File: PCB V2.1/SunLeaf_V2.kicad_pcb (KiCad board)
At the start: 4 copper layers, 77.5 x 40 mm, 121 parts, among them IC1 ESP_09, J1 20021121-00010C4LF, J10 B4B-PH-K-S(LF)(SN), J11 B4B-PH-K-S(LF)(SN), J12 B4B-PH-K-S(LF)(SN), J13 B4B-PH-K-S(LF)(SN), J14 B4B-PH-K-S(LF)(SN), J15 B4B-PH-K-S(LF)(SN), J16 B4B-PH-K-S(LF)(SN), J2 0475890001-MicroUSBPort, J3 B2B-PH-K-S(LF)(SN), J4 B3B-PH-K-S(LF)(SN), J5 B4B-PH-K-S(LF)(SN), J6 B4B-PH-K-S(LF)(SN), J7 B4B-PH-K-S(LF)(SN), J8 B4B-PH-K-S(LF)(SN), J9 B4B-PH-K-S(LF)(SN), P1 CONN_01X04, P2 CONN_01X03, Q1 DMG2307L-7, Q2 DMG2307L-7, SW1 B3U-1000P, SW2 B3U-1000P, T1 1909763-1, U1 STM32F446RET6_-_TQFP64, U2 BQ24210DQCT, U3 AZ1117CR-3.3TRG1_1, U4 74HC4052D, U5 PCA9518DBQR, X1 ABM3B8.000MHZB2T, X2 ABS07-32.768KHZ-9-T

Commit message: Schematic Changes
Schematic changes saved.
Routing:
- net (no net): track 30.7 -> 0.00 mm, vias 10 -> 0
- net GND: track 256.5 -> 275.0 mm, vias 130 -> 141
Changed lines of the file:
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@@
     (links 309)
     (no_connects 7)
-    (area 42.949999 29.949999 120.550001 70.050001)
+    (area 21.000001 17.300001 134.897448 87.526447)
     (thickness 1.6)
     (drawings 165)
-    (tracks 1376)
+    (tracks 1365)
     (zones 0)
     (modules 121)
@@
     (40 Dwgs.User user)
     (41 Cmts.User user)
-    (42 Eco1.User user hide)
+    (42 Eco1.User user)
     (43 Eco2.User user)
     (44 Edge.Cuts user)
@@
   (gr_line (start 120.5 30) (end 43 30) (layer Edge.Cuts) (width 0.1))
   (gr_line (start 120.5 30) (end 120.5 70) (layer Edge.Cuts) (width 0.1))
-  (segment (start 77.597 61.214) (end 77.597 61.86384) (width 0.1778) (layer F.Cu) (net 0))
-  (segment (start 77.597 61.86384) (end 76.232752 63.228088) (width 0.1778) (layer F.Cu) (net 0))
-  (segment (start 79.248 58.039) (end 78.359 58.039) (width 0.1778) (layer F.Cu) (net 0))
-  (via (at 79.248 58.039) (size 0.635) (drill 0.3302) (layers F.Cu B.Cu) (net 0))
-  (segment (start 77.597 59.182) (end 77.597 58.801) (width 0.1778) (layer F.Cu) (net 0))
-  (segment (start 77.597 58.801) (end 78.359 58.039) (width 0.1778) (layer F.Cu) (net 0))
-  (via (at 78.359 58.039) (size 0.635) (drill 0.3302) (layers F.Cu B.Cu) (net 0))
-  (segment (start 78.359 60.325) (end 78.359 60.452) (width 0.1778) (layer F.Cu) (net 0))
-  (segment (start 78.359 60.452) (end 77.597 61.214) (width 0.1778) (layer F.Cu) (net 0))
-  (segment (start 79.375 60.325) (end 78.359 60.325) (width 0.1778) (layer F.Cu) (net 0))
-  (via (at 79.375 60.325) (size 0.635) (drill 0.3302) (layers F.Cu B.Cu) (net 0))
-  (via (at 78.359 60.325) (size 0.635) (drill 0.3302) (layers F.Cu B.Cu) (net 0))
-  (segment (start 75.438 54.991) (end 75.438 55.118) (width 0.1778) (layer F.Cu) (net 0))
-  (segment (start 75.438 55.118) (end 76.327 56.007) (width 0.1778) (layer F.Cu) (net 0))
-  (segment (start 75.438 53.975) (end 75.438 54.991) (width 0.1778) (layer F.Cu) (net 0))
-  (via (at 75.438 53.975) (size 0.635) (drill 0.3302) (layers F.Cu B.Cu) (net 0))
-  (via (at 75.438 54.991) (size 0.635) (drill 0.3302) (layers F.Cu B.Cu) (net 0))
-  (segment (start 73.152 54.991) (end 73.152 54.102) (width 0.1778) (layer B.Cu) (net 0))
-  (via (at 73.152 54.102) (size 0.635) (drill 0.3302) (layers F.Cu B.Cu) (net 0))
-  (segment (start 74.295 56.007) (end 74.168 56.007) (width 0.1778) (layer F.Cu) (net 0))
-  (segment (start 74.168 56.007) (end 73.152 54.991) (width 0.1778) (layer F.Cu) (net 0))
-  (via (at 73.152 54.991) (size 0.635) (drill 0.3302) (layers F.Cu B.Cu) (net 0))
-  (segment (start 70.811612 54.864) (end 70.811612 53.99643) (width 0.1778) (layer B.Cu) (net 0))
-  (via (at 70.811612 53.99643) (size 0.635) (drill 0.3302) (layers F.Cu B.Cu) (net 0))
-  (segment (start 71.12 57.15) (end 71.12 55.172388) (width 0.1778) (layer F.Cu) (net 0))
-  (segment (start 71.12 55.172388) (end 70.811612 54.864) (width 0.1778) (layer F.Cu) (net 0))
-  (via (at 70.811612 54.864) (size 0.635) (drill 0.3302) (layers F.Cu B.Cu) (net 0))
-  (segment (start 77.597 59.182) (end 77.597 59.631012) (width 0.1778) (layer F.Cu) (net 0))
-  (segment (start 77.597 59.631012) (end 77.597 61.214) (width 0.1778) (layer F.Cu) (net 0))
-  (segment (start 77.597 57.15) (end 77.47 57.15) (width 0.1778) (layer F.Cu) (net 0))
-  (segment (start 77.47 57.15) (end 76.327 56.007) (width 0.1778) (layer F.Cu) (net 0))
-  (segment (start 72.263 56.388) (end 73.914 56.388) (width 0.1778) (layer F.Cu) (net 0))
-  (segment (start 73.914 56.388) (end 74.295 56.007) (width 0.1778) (layer F.Cu) (net 0))
-  (segment (start 71.12 59.182) (end 71.12 57.15) (width 0.1778) (layer F.Cu) (net 0))
-  (segment (start 71.12 59.182) (end 71.12 61.087) (width 0.1778) (layer F.Cu) (net 0))
-  (segment (start 72.263 56.388) (end 71.882 56.388) (width 0.1778) (layer F.Cu) (net 0))
-  (segment (start 71.882 56.388) (end 71.12 57.15) (width 0.1778) (layer F.Cu) (net 0))
-  (segment (start 76.327 56.007) (end 74.295 56.007) (width 0.1778) (layer F.Cu) (net 0))
-  (segment (start 77.597 59.182) (end 77.597 57.15) (width 0.1778) (layer F.Cu) (net 0))
   (via (at 61.671682 53.343897) (size 0.635) (drill 0.3302) (layers F.Cu B.Cu) (net 1))
   (segment (start 61.7474 53.8476) (end 61.7474 53.419615) (width 0.1778) (layer F.Cu) (net 1))
@@
   (segment (start 54.0004 66.8528) (end 54.356 66.4972) (width 0.1778) (layer F.Cu) (net 1))
   (via (at 54.356 66.4972) (size 0.635) (drill 0.3302) (layers F.Cu B.Cu) (net 1))
+  (segment (start 72.284225 57.184946) (end 71.281946 57.184946) (width 0.1778) (layer F.Cu) (net 2))
+  (segment (start 71.281946 57.184946) (end 71.247 57.15) (width 0.1778) (layer F.Cu) (net 2))
+  (via (at 71.247 57.15) (size 0.635) (drill 0.3302) (layers F.Cu B.Cu) (net 2))
+  (segment (start 70.993 55.245) (end 70.993 54.102) (width 0.1778) (layer B.Cu) (net 2))
+  (via (at 70.993 54.102) (size 0.635) (drill 0.3302) (layers F.Cu B.Cu) (net 2))
+  (segment (start 72.284225 57.184946) (end 70.993 55.893721) (width 0.1778) (layer F.Cu) (net 2))
+  (segment (start 70.993 55.893721) (end 70.993 55.245) (width 0.1778) (layer F.Cu) (net 2))
+  (via (at 70.993 55.245) (size 0.635) (drill 0.3302) (layers F.Cu B.Cu) (net 2))
+  (segment (start 73.152 54.229) (end 73.152 55.626) (width 0.1778) (layer F.Cu) (net 2))
+  (via (at 73.152 54.229) (size 0.635) (drill 0.3302) (layers F.Cu B.Cu) (net 2))
+  (segment (start 74.25226 57.166251) (end 73.152 56.065991) (width 0.1778) (layer F.Cu) (net 2))
+  (segment (start 73.152 56.065991) (end 73.152 55.626) (width 0.1778) (layer F.Cu) (net 2))
+  (via (at 73.152 55.626) (size 0.635) (drill 0.3302) (layers F.Cu B.Cu) (net 2))
+  (segment (start 75.438 53.975) (end 75.438 55.245) (width 0.1778) (layer F.Cu) (net 2))
+  (via (at 75.438 53.975) (size 0.635) (drill 0.3302) (layers F.Cu B.Cu) (net 2))
+  (segment (start 76.265361 57.161389) (end 76.265361 56.072361) (width 0.1778) (layer F.Cu) (net 2))
+  (segment (start 76.265361 56.072361) (end 75.438 55.245) (width 0.1778) (layer F.Cu) (net 2))
+  (via (at 75.438 55.245) (size 0.635) (drill 0.3302) (layers F.Cu B.Cu) (net 2))
+  (segment (start 79.121 58.166) (end 78.232 58.166) (width 0.1778) (layer F.Cu) (net 2))
+  (via (at 79.121 58.166) (size 0.635) (drill 0.3302) (layers F.Cu B.Cu) (net 2))
+  (segment (start 76.265361 57.161389) (end 77.227389 57.161389) (width 0.1778) (layer F.Cu) (net 2))
+  (segment (start 77.227389 57.161389) (end 78.232 58.166) (width 0.1778) (layer F.Cu) (net 2))
+  (via (at 78.232 58.166) (size 0.635) (drill 0.3302) (layers F.Cu B.Cu) (net 2))
+  (segment (start 79.502 60.198) (end 78.359 60.198) (width 0.1778) (layer F.Cu) (net 2))
+  (via (at 79.502 60.198) (size 0.635) (drill 0.3302) (layers F.Cu B.Cu) (net 2))
+  (segment (start 76.274175 61.192843) (end 77.364157 61.192843) (width 0.1778) (layer F.Cu) (net 2))
+  (segment (start 77.364157 61.192843) (end 78.359 60.198) (width 0.1778) (layer F.Cu) (net 2))
+  (via (at 78.359 60.198) (size 0.635) (drill 0.3302) (layers F.Cu B.Cu) (net 2))
   (segment (start 80.518 62.992) (end 79.112 64.398) (width 0.1778) (layer F.Cu) (net 2))
   (segment (start 79.112 64.398) (end 79.0601 64.398) (width 0.1778) (layer F.Cu) (net 2))

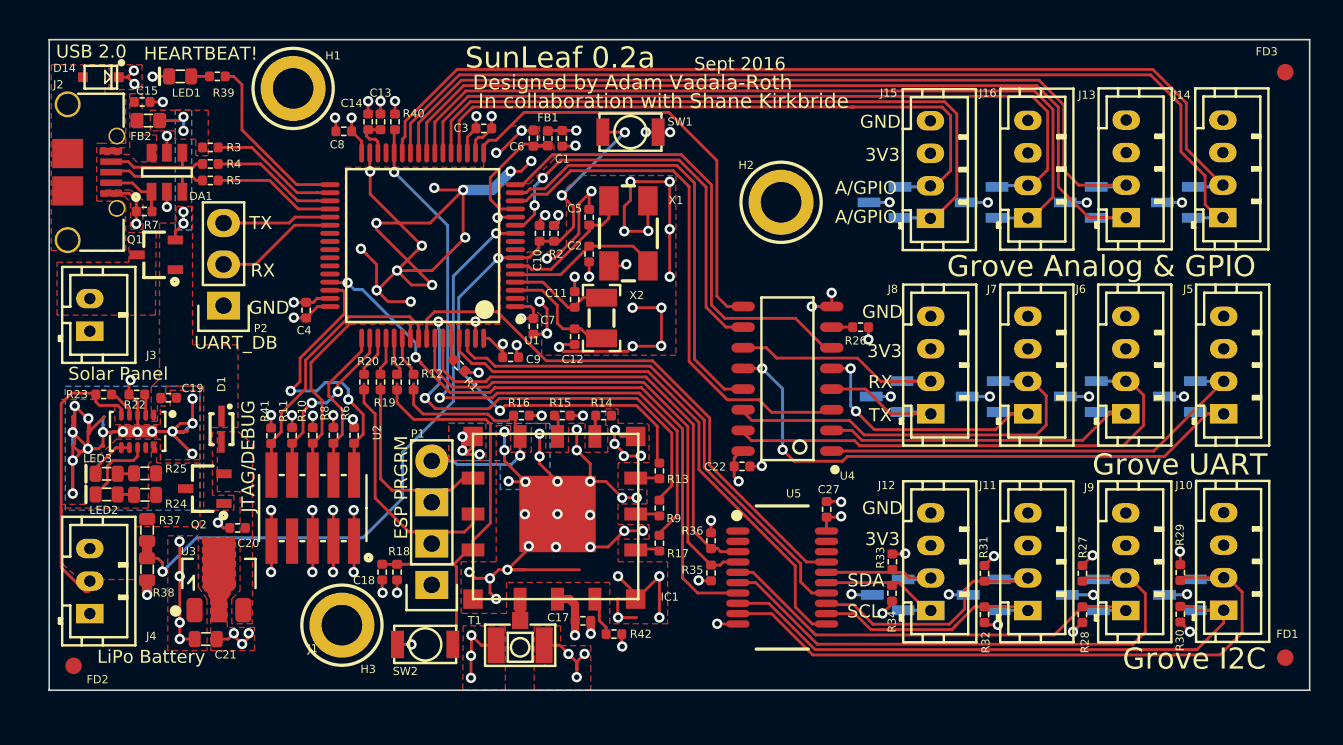
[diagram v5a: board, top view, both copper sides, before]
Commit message: Test Points
Test points added as well as some retooling of the PCB overall. More
updates to come before the pending fab
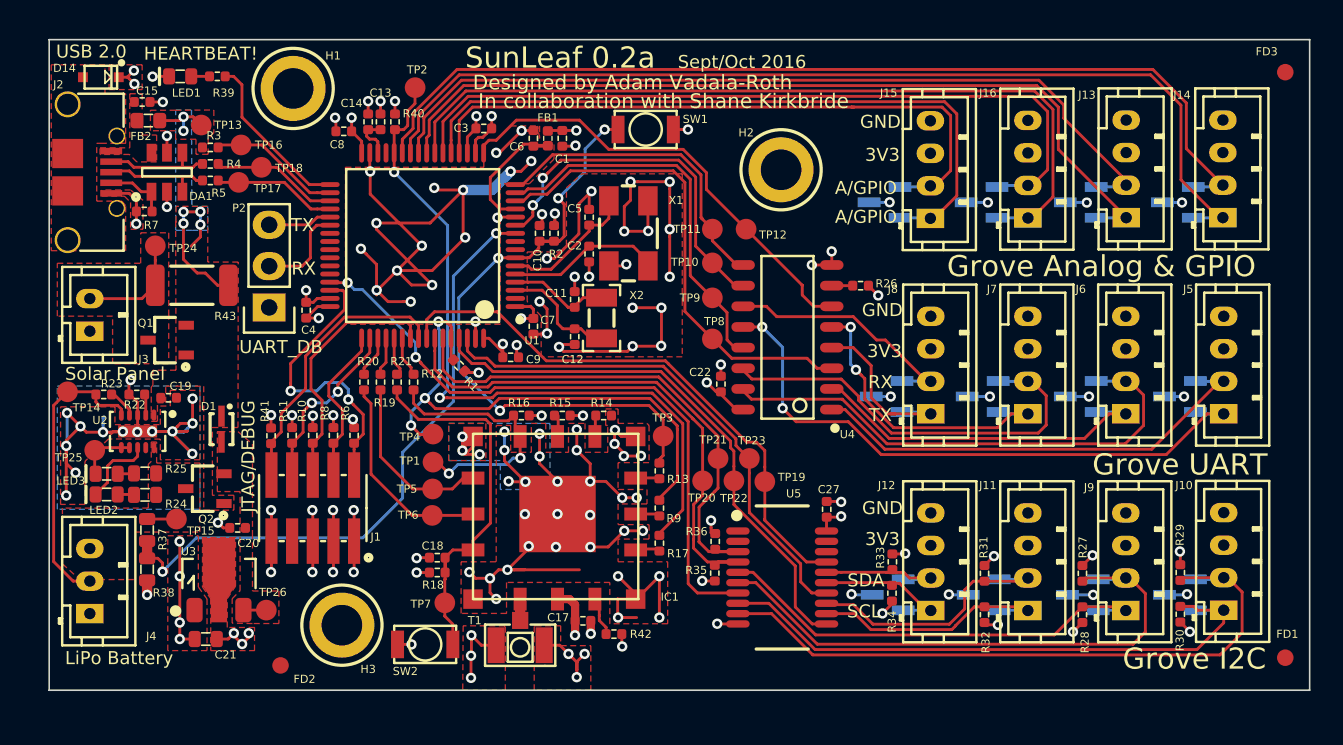
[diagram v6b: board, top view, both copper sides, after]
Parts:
- removed P1: CONN_01X04, Pin_Headers:Pin_Header_Straight_1x04
- added R43: RC5025J000CS, PCB_Footprints:R2010, F.Cu at (51.8, 45.1)
- added TP1: TEST_POINT, PCB_Footprints:TEST_POINT, F.Cu at (66.6, 56.0)
- added TP10: TEST_POINT, PCB_Footprints:TEST_POINT, F.Cu at (83.8, 43.7)
- added TP11: TEST_POINT, PCB_Footprints:TEST_POINT, F.Cu at (83.8, 41.6)
- added TP12: TEST_POINT, PCB_Footprints:TEST_POINT, F.Cu at (85.8, 41.6)
- added TP13: TEST_POINT, PCB_Footprints:TEST_POINT, F.Cu at (52.4, 35.2)
- added TP14: TEST_POINT, PCB_Footprints:TEST_POINT, F.Cu at (44.1, 51.6)
- added TP15: TEST_POINT, PCB_Footprints:TEST_POINT, F.Cu at (50.8, 59.5)
- added TP16: TEST_POINT, PCB_Footprints:TEST_POINT, F.Cu at (54.8, 36.5)
- added TP17: TEST_POINT, PCB_Footprints:TEST_POINT, F.Cu at (54.6, 38.8)
- added TP18: TEST_POINT, PCB_Footprints:TEST_POINT, F.Cu at (56.0, 37.9)
- added TP19: TEST_POINT, PCB_Footprints:TEST_POINT, F.Cu at (87.0, 57.2)
- added TP2: TEST_POINT, PCB_Footprints:TEST_POINT, F.Cu at (65.5, 33.0)
- added TP20: TEST_POINT, PCB_Footprints:TEST_POINT, F.Cu at (83.2, 57.1)
- added TP21: TEST_POINT, PCB_Footprints:TEST_POINT, F.Cu at (84.1, 55.8)
- added TP22: TEST_POINT, PCB_Footprints:TEST_POINT, F.Cu at (85.1, 57.1)
- added TP23: TEST_POINT, PCB_Footprints:TEST_POINT, F.Cu at (86.0, 55.8)
- added TP24: TEST_POINT, PCB_Footprints:TEST_POINT, F.Cu at (49.5, 42.7)
- added TP25: TEST_POINT, PCB_Footprints:TEST_POINT, F.Cu at (45.8, 55.2)
- added TP26: TEST_POINT, PCB_Footprints:TEST_POINT, F.Cu at (56.4, 65.1)
- added TP3: TEST_POINT, PCB_Footprints:TEST_POINT, F.Cu at (80.8, 54.4)
- added TP4: TEST_POINT, PCB_Footprints:TEST_POINT, F.Cu at (66.6, 54.2)
- added TP5: TEST_POINT, PCB_Footprints:TEST_POINT, F.Cu at (66.6, 57.6)
- added TP6: TEST_POINT, PCB_Footprints:TEST_POINT, F.Cu at (66.5, 59.2)
- added TP7: TEST_POINT, PCB_Footprints:TEST_POINT, F.Cu at (67.3, 64.6)
- added TP8: TEST_POINT, PCB_Footprints:TEST_POINT, F.Cu at (83.8, 48.4)
- added TP9: TEST_POINT, PCB_Footprints:TEST_POINT, F.Cu at (83.8, 45.9)
- R14, R15, R16: value RC1005F102CS -> RC1005F103CS
- moved FD2 12.7 mm to (57.2, 68.5)
- moved Q1 5.29 mm to (50.2, 48.5)
- moved C22 5.22 mm to (84.3, 51.2), turned to 90 degrees
- moved C18 3.50 mm to (66.9, 61.8), turned to 180 degrees
- moved P2 2.81 mm to (56.5, 46.5)
- moved R26 2.55 mm to (92.9, 45.1)
- moved U4 2.55 mm to (88.4, 48.3)
- moved R18 2.47 mm to (66.9, 62.8), turned to 0 degrees
- moved H2 2.00 mm to (88.0, 38.0)
- moved SW1 0.95 mm to (79.7, 35.5)
- moved R36 0.26 mm to (84.0, 60.9)
- moved R35 0.23 mm to (83.9, 62.8)
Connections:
- U1 pad 16: /MCU-STM32F446RET6/USW_EN -> /MCU-STM32F446RET6/USW_S1
- U1 pad 17: /MCU-STM32F446RET6/USW_S1 -> /MCU-STM32F446RET6/USW_EN
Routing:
- net GND: track 275.0 -> 261.8 mm, vias 141 -> 139
- net /MCU-STM32F446RET6/VBUS: track 4.35 -> 13.5 mm, vias 4 -> 6
- net Net-(J3-Pad2): track 0.00 -> 6.79 mm
- net /MCU-STM32F446RET6/USW_S1: track 27.1 -> 20.5 mm
- net /MCU-STM32F446RET6/ESPTOST_BOOT0: track 29.2 -> 33.4 mm, vias 2 -> 3
- net /MCU-STM32F446RET6/ESPTOST_BOOT1: track 40.5 -> 44.7 mm
- net /UART Grove Sensors/UART_S_RX: track 33.7 -> 30.3 mm
- net /I2C Grove Sensors/I2C_SDA: track 28.8 -> 31.9 mm
- net /MCU-STM32F446RET6/UART_S_RX: track 26.7 -> 23.8 mm
- net /MCU-STM32F446RET6/UART6_TX: track 6.69 -> 3.93 mm
- net Net-(C18-Pad1): track 27.3 -> 24.8 mm
- net /MCU-STM32F446RET6/USW_S0: track 25.3 -> 22.8 mm
- net Net-(IC1-Pad11): track 15.6 -> 13.2 mm
- net /UART Grove Sensors/UART_TX3: track 8.53 -> 10.9 mm
- net /I2C Grove Sensors/I2C_SCL: track 30.0 -> 32.4 mm
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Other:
- board text added: "Sept/Oct 2016"
- board text removed: "ESP PRGRM"
- board text removed: "ESP_PGM_MODE"
- board text removed: "ESP_RX"
- board text removed: "ESP_TX"
- board text removed: "Sept 2016"

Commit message: JTAG Test Points
Test Points added to JTAG.
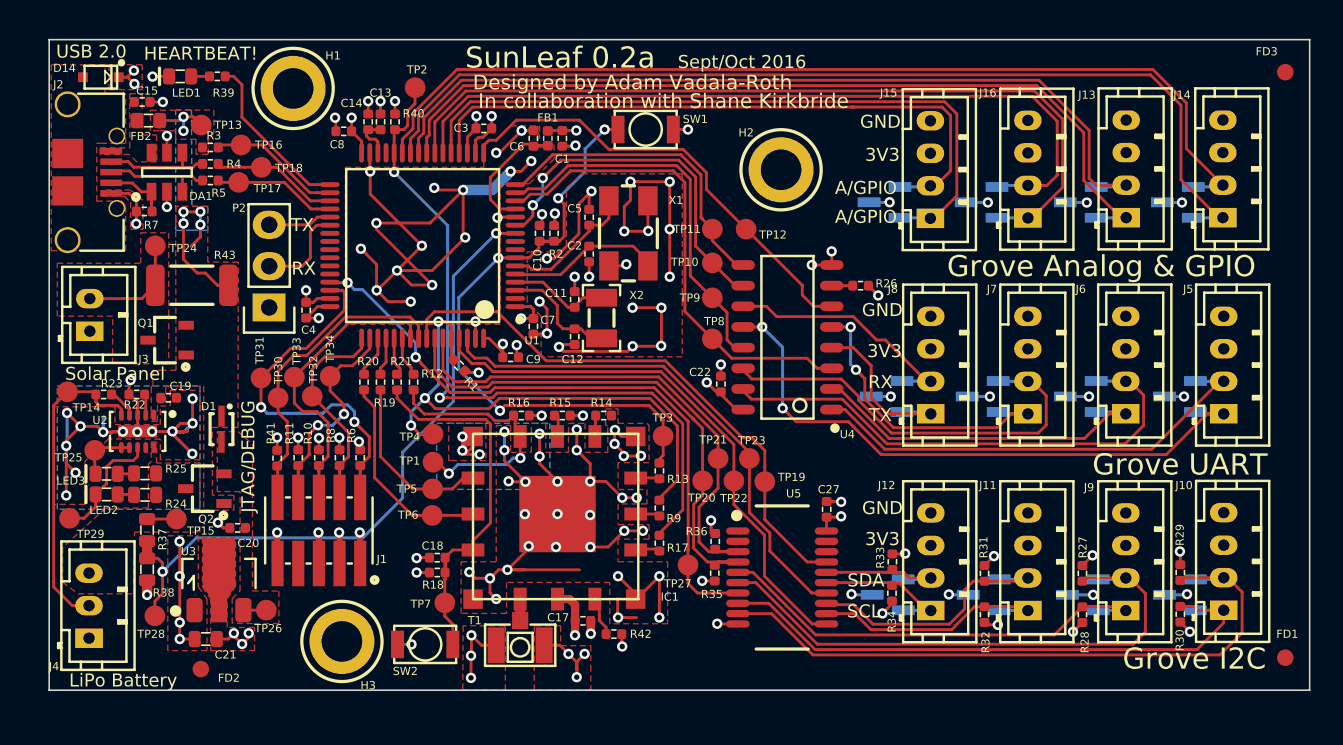
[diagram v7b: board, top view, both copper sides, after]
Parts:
- added TP27: TEST_POINT, PCB_Footprints:TEST_POINT, F.Cu at (82.3, 62.3)
- added TP28: TEST_POINT, PCB_Footprints:TEST_POINT, F.Cu at (49.5, 65.4)
- added TP29: TEST_POINT, PCB_Footprints:TEST_POINT, F.Cu at (44.2, 59.4)
- added TP30: TEST_POINT, PCB_Footprints:TEST_POINT, F.Cu at (57.1, 52.0)
- added TP31: TEST_POINT, PCB_Footprints:TEST_POINT, F.Cu at (56.0, 50.8)
- added TP32: TEST_POINT, PCB_Footprints:TEST_POINT, F.Cu at (59.2, 51.9)
- added TP33: TEST_POINT, PCB_Footprints:TEST_POINT, F.Cu at (58.1, 50.8)
- added TP34: TEST_POINT, PCB_Footprints:TEST_POINT, F.Cu at (60.3, 50.7)
- moved FD2 4.91 mm to (52.3, 68.7)
- moved J4 1.51 mm to (45.5, 66.8)
- moved J1 1.43 mm to (59.6, 60.2)
- moved R10 1.43 mm to (59.6, 55.7)
- moved R11 1.43 mm to (58.3, 55.7)
- moved R41 1.43 mm to (57.0, 55.7)
- moved R6 1.43 mm to (62.1, 55.7)
- moved R8 1.43 mm to (60.9, 55.7)
- moved H3 1.00 mm to (61.0, 67.0)
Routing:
- net GND: track 261.8 -> 256.1 mm, vias 139 -> 136
- net /MCU-STM32F446RET6/SWDIO_TMS: track 18.2 -> 23.0 mm
- net /MCU-STM32F446RET6/SWCLK_TCK: track 9.93 -> 13.3 mm
- net /MCU-STM32F446RET6/BAT_VOLT: track 39.1 -> 42.0 mm
- net /MCU-STM32F446RET6/SWO_TDO: track 15.6 -> 18.4 mm
- net Net-(LED2-Pad2): track 4.68 -> 7.33 mm
- net /MCU-STM32F446RET6/SWO_TDI: track 10.9 -> 13.3 mm
- net /MCU-STM32F446RET6/NJTRST: track 17.1 -> 19.4 mm
- net +3V3: track 45.7 -> 43.8 mm, vias 35 -> 34
- net /Power-System/THERM: track 18.1 -> 19.6 mm
- net /Analog and Digital Grove IO/ANIO_0: track 51.6 -> 52.9 mm
- net /Analog and Digital Grove IO/ANIO_6: track 47.3 -> 48.3 mm
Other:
- board text removed: "UART_DB"
